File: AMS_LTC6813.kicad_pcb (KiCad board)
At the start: 2 copper layers, 205 parts, among them J1 Conn_01x06, J10 Conn_01x02_Male, J11 Conn_01x02_Male, J12 Conn_01x02_Male, J13 Conn_01x02_Male, J14 Conn_01x02_Male, J15 Conn_01x02_Male, J16 Conn_01x02_Male, J17 Conn_01x02_Male, J18 Conn_01x02_Male, J19 Conn_01x02_Male, J2 Conn_01x03_Female, J20 Conn_01x02_Male, J21 Conn_01x02_Male, J22 Conn_01x02_Male, J23 Conn_01x02_Male, J24 Conn_01x02_Male, J25 Conn_01x02_Male, J26 Conn_01x02_Male, J27 Conn_01x02_Male, J28 Conn_01x02_Male, J29 Conn_01x02_Male, J3 Conn_01x06, J30 Conn_01x02_Male, J31 Conn_01x02_Male, J32 Conn_01x02_Male, J33 Conn_01x02_Male, J34 Conn_01x02_Male, J35 Conn_01x02_Male, J36 Conn_01x02_Male, J37 Conn_01x02_Male, J38 Conn_01x02_Male, J39 Conn_01x02_Male, J4 Conn_02x02_Counter_Clockwise, J40 Conn_01x02_Male, J41 Conn_01x02_Male, J42 Conn_01x02_Male, J43 Conn_01x02_Male, J44 Conn_01x02_Male, J45 Conn_01x02_Male, J46 Conn_01x02_Male, J47 Conn_01x02_Male, J48 Conn_01x02_Male, J49 Conn_01x02_Male, J5 Conn_01x02_Male, J50 Conn_01x02_Male, J51 Conn_01x02_Male, J52 Conn_01x02_Male, J53 Conn_01x02_Male, J54 Conn_01x02_Male, J55 Conn_01x02_Male, J56 Conn_01x02_Male, J57 Conn_01x02_Male, J58 Conn_01x02_Male, J59 Conn_01x02_Male, J6 Conn_01x02_Male, J60 Conn_01x02_Male, J61 Conn_01x02_Male, J62 Conn_01x02_Male, J63 Conn_01x02_Male, J64 Conn_01x02_Male, J65 Conn_01x02_Male, J66 Conn_01x02_Male, J67 Conn_01x02_Male, J68 Conn_01x02_Male, J69 Conn_02x02_Counter_Clockwise, J7 Conn_01x02_Male, J70 Conn_01x03_Female, J71 Conn_02x20_Counter_Clockwise, J72 Conn_01x02_Male, J73 Conn_01x02_Male, J74 Conn_01x02_Male, J75 Conn_01x02_Male, J76 Conn_01x02_Male, J77 Conn_01x02_Male, J78 Conn_01x02_Male, J79 Conn_01x02_Male, J8 Conn_01x02_Male, J80 Conn_01x02_Male, J81 Conn_01x02_Male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

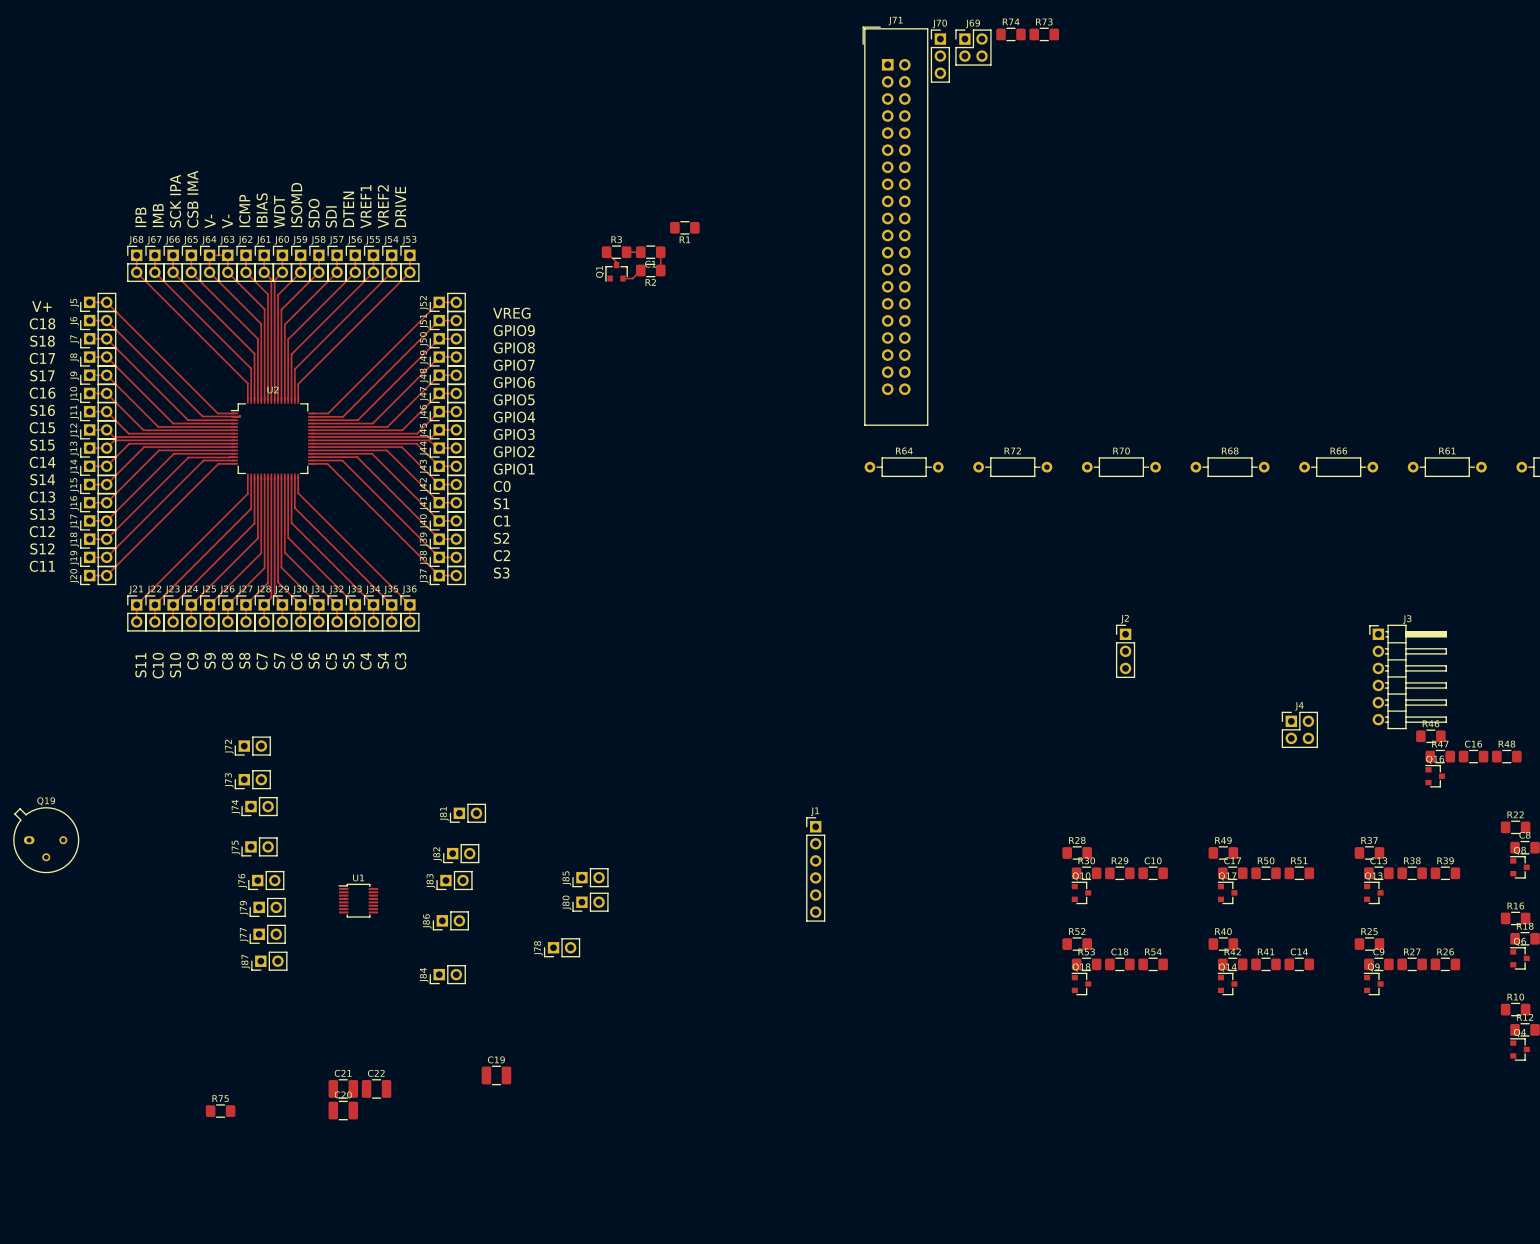
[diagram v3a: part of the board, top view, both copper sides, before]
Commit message: tout route sauf voltage channel
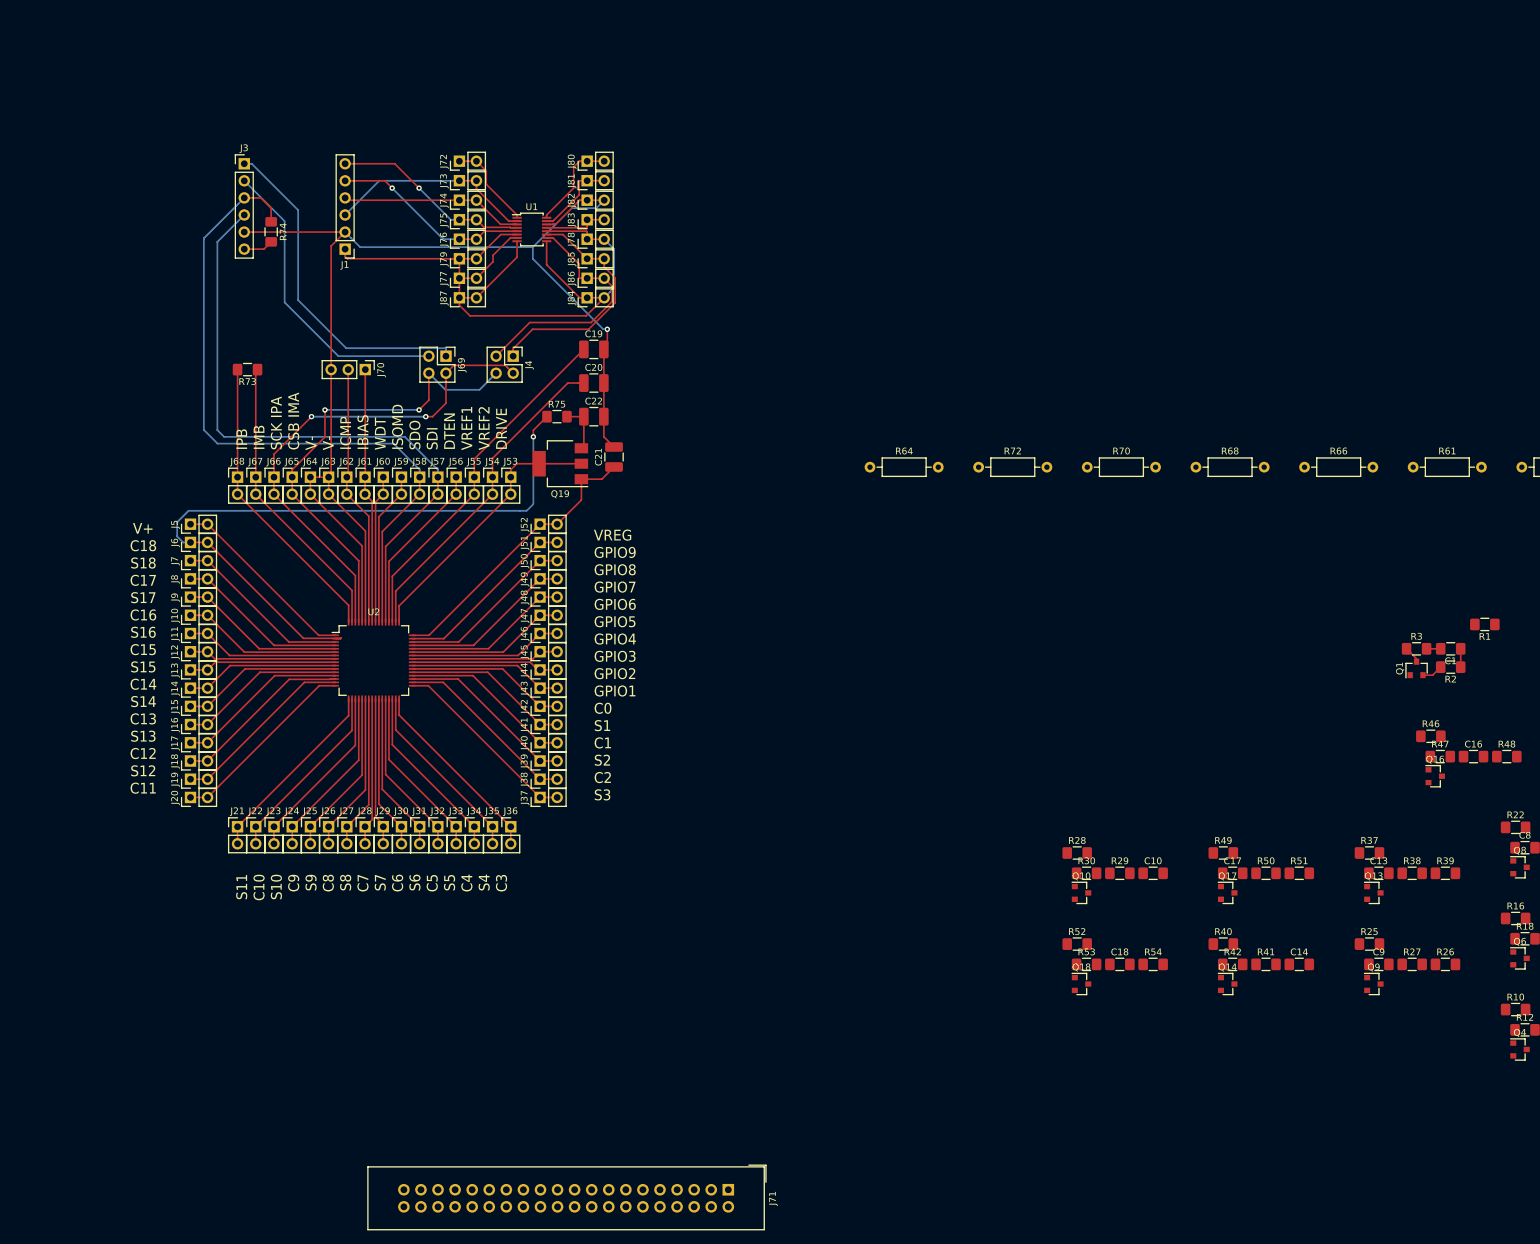
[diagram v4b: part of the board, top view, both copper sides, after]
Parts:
- removed J2: Conn_01x03_Female, Connector_PinHeader_2.54mm:PinHeader_1x03_P2.54mm_Vertical
- J3: footprint Connector_PinHeader_2.54mm:PinHeader_1x06_P2.54mm_Horizontal -> Connector_PinHeader_2.54mm:PinHeader_1x06_P2.54mm_Vertical
- Q19: footprint Package_TO_SOT_THT:TO-39-3 -> Package_TO_SOT_SMD:SOT-223-3_TabPin2
- moved J3 182.6 mm to (64.0, 32.4)
- moved J71 169.0 mm to (136.0, 185.0), turned to 270 degrees
- moved C1 132.8 mm to (243.5, 104.5)
- moved Q1 132.8 mm to (238.4, 107.5)
- moved R1 132.8 mm to (248.5, 100.9)
- moved R2 132.8 mm to (243.5, 107.3)
- moved R3 132.8 mm to (238.4, 104.5)
- moved R73 128.6 mm to (64.5, 63.0), turned to 180 degrees
- moved J4 127.9 mm to (104.0, 61.0), turned to 270 degrees
- moved R75 114.8 mm to (110.5, 70.0)
- moved C20 114.5 mm to (116.0, 65.0)
- moved R74 113.9 mm to (68.0, 42.5), turned to 270 degrees
- moved J1 110.8 mm to (79.0, 45.1), turned to 180 degrees
- moved J80 110.2 mm to (115.0, 32.0)
- moved C19 109.0 mm to (116.0, 60.0)
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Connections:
- J1 pad 6: /SCk -> /SCK
- J4 pad 1: /SCKIPA -> /IP
- J4 pad 2: /CSBIMA -> /SCKIPA
- J4 pad 4: /IP -> /CSBIMA
- J69 pad 1: /SCKIPA -> /SCKIPA1
- J69 pad 2: /CSBIMA -> /SCKIPA
- J69 pad 4: /SCKIPA1 -> /CSBIMA
- J70 pad 1: /IBIAS1 -> /IBIAS
- J70 pad 2: /ICMB1 -> /ICMP
- J70 pad 3: /GND1 -> /C0
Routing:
- net /C0: track 75.2 -> 215.6 mm, vias 0 -> 1
- net /VDD1: track 0.00 -> 117.3 mm
- net /SDO: track 23.9 -> 103.2 mm
- net /C18: track 32.0 -> 104.4 mm, vias 0 -> 1
- net /SDI: track 24.8 -> 94.8 mm
- net /SCKIPA1: track 0.00 -> 50.3 mm
- net /SCKIPA: track 26.6 -> 74.2 mm, vias 0 -> 2
- net /CSBIMA1: track 0.00 -> 45.3 mm
- net /CSBIMA: track 25.7 -> 69.8 mm, vias 0 -> 2
- net /IM: track 0.00 -> 36.8 mm
- net /IP: track 0.00 -> 36.4 mm
- net /MOSI: track 0.00 -> 30.9 mm
- net /CS: track 0.00 -> 29.7 mm, vias 0 -> 1
- net /SCK: track 0.00 -> 29.5 mm, vias 0 -> 1
- net /MISO: track 0.00 -> 27.2 mm
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
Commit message: voltages partiellements route
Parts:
- moved R59 264.6 mm to (29.0, 113.0), turned to 180 degrees
- moved R56 259.0 mm to (29.0, 97.0), turned to 180 degrees
- moved R62 257.3 mm to (59.0, 158.0), turned to 270 degrees
- moved R21 252.8 mm to (42.5, 124.6), turned to 180 degrees
- moved R55 251.7 mm to (29.0, 91.0), turned to 180 degrees
- moved C3 248.4 mm to (42.5, 99.3), turned to 180 degrees
- moved R60 247.8 mm to (29.0, 119.0), turned to 180 degrees
- moved R6 247.3 mm to (42.5, 96.5), turned to 180 degrees
- moved R65 247.1 mm to (77.0, 158.0), turned to 270 degrees
- moved C5 244.8 mm to (42.5, 110.6), turned to 180 degrees
- moved R5 244.2 mm to (51.5, 93.7), turned to 180 degrees
- moved C2 243.3 mm to (42.5, 93.7), turned to 180 degrees
- moved R58 243.2 mm to (29.0, 108.0), turned to 180 degrees
- moved C7 242.9 mm to (42.5, 121.8), turned to 180 degrees
- moved R15 239.6 mm to (42.5, 113.4), turned to 180 degrees
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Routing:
- net /C2: track 27.5 -> 76.8 mm
- net /C1: track 25.7 -> 73.0 mm
- net /C0: track 215.6 -> 236.3 mm
- net /C12: track 26.6 -> 47.1 mm
- net /C16: track 23.8 -> 43.9 mm
- net /C15: track 22.0 -> 42.1 mm
- net /C14: track 23.0 -> 43.0 mm
- net /C17: track 27.8 -> 45.8 mm
- net /C13: track 24.8 -> 42.1 mm
- net /C3: track 28.4 -> 42.6 mm
- net Net-(Q15-Pad3): track 0.00 -> 11.1 mm
- net Net-(Q18-Pad3): track 0.00 -> 10.7 mm
- net /C18: track 104.4 -> 114.9 mm
- net Net-(Q17-Pad3): track 0.00 -> 10.5 mm
- net /CELL3: track 0.00 -> 3.75 mm
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
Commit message: routing everything
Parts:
- moved J71 82.0 mm to (54.6, 175.3), turned to 90 degrees
- moved R61 33.5 mm to (38.1, 157.5), turned to 270 degrees
- moved R60 27.3 mm to (38.1, 144.8), turned to 270 degrees
- moved C18 23.2 mm to (98.8, 152.2)
- moved R72 23.1 mm to (101.8, 156.7)
- moved R54 23.1 mm to (101.8, 152.2)
- moved C15 23.0 mm to (104.9, 152.2)
- moved R45 23.0 mm to (108.0, 152.2)
- moved R69 23.0 mm to (108.0, 156.7)
- moved Q15 22.9 mm to (106.9, 147.5)
- moved R43 22.9 mm to (108.0, 143.2)
- moved R44 22.7 mm to (104.9, 143.2)
- moved R52 22.6 mm to (101.8, 143.2)
- moved Q18 22.6 mm to (100.7, 147.5)
- moved R53 22.5 mm to (98.8, 143.2)
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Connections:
- J71 pad 10: /CELL10 -> /CELL14
- J71 pad 11: /CELL9 -> Net-(J71-Pad11)
- J71 pad 12: /CELL8 -> /CELL13
- J71 pad 13: /CELL7 -> Net-(J71-Pad13)
- J71 pad 14: /CELL6 -> /CELL12
- J71 pad 15: /CELL5 -> Net-(J71-Pad15)
- J71 pad 16: /CELL4 -> /CELL11
- J71 pad 17: /CELL3 -> Net-(J71-Pad17)
- J71 pad 18: /CELL2 -> /CELL10
- J71 pad 19: /CELL1 -> Net-(J71-Pad19)
- J71 pad 20: /C0 -> /CELL9
- J71 pad 21: /GPIO1 -> Net-(J71-Pad21)
- J71 pad 22: /GPIO2 -> /CELL8
- J71 pad 23: /GPIO3 -> /GPIO9
- J71 pad 24: /GPIO4 -> /CELL7
- J71 pad 25: /GPIO5 -> /GPIO8
- J71 pad 26: /GPIO6 -> /CELL6
- J71 pad 28: /GPIO8 -> /CELL5
- J71 pad 29: /GPIO9 -> /GPIO6
- J71 pad 3: /CELL17 -> Net-(J71-Pad3)
- J71 pad 30: Net-(J71-Pad30) -> /CELL4
- J71 pad 31: Net-(J71-Pad31) -> /GPIO5
- J71 pad 32: Net-(J71-Pad32) -> /CELL3
- J71 pad 33: Net-(J71-Pad33) -> /GPIO4
- J71 pad 34: Net-(J71-Pad34) -> /CELL2
- J71 pad 35: Net-(J71-Pad35) -> /GPIO3
- J71 pad 36: Net-(J71-Pad36) -> /CELL1
- J71 pad 37: Net-(J71-Pad37) -> /GPIO2
- J71 pad 38: Net-(J71-Pad38) -> /C0
- J71 pad 39: Net-(J71-Pad39) -> /GPIO1
- J71 pad 4: /CELL16 -> /CELL17
- J71 pad 5: /CELL15 -> Net-(J71-Pad5)
- J71 pad 6: /CELL14 -> /CELL16
- J71 pad 7: /CELL13 -> Net-(J71-Pad7)
- J71 pad 8: /CELL12 -> /CELL15
- J71 pad 9: /CELL11 -> Net-(J71-Pad9)
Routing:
- net /GPIO9: track 27.5 -> 144.0 mm
- net /GPIO8: track 26.6 -> 136.7 mm
- net /GPIO7: track 25.7 -> 129.4 mm
- net /GPIO5: track 23.8 -> 121.5 mm
- net /GPIO6: track 24.7 -> 122.1 mm
- net /CELL18: track 2.29 -> 97.1 mm, vias 0 -> 1
- net /GPIO4: track 22.9 -> 114.2 mm
- net /CELL17: track 2.26 -> 92.7 mm, vias 0 -> 1
- net /GPIO3: track 22.0 -> 106.9 mm
- net /CELL16: track 2.24 -> 86.3 mm, vias 0 -> 1
- net /CELL15: track 2.21 -> 82.1 mm, vias 0 -> 1
- net /GPIO2: track 22.0 -> 100.6 mm
- net /CELL14: track 2.18 -> 74.1 mm, vias 0 -> 1
- net /GPIO1: track 23.0 -> 93.8 mm
- net /CELL13: track 2.16 -> 69.6 mm, vias 0 -> 1
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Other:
- board outline added: 94 x 165.2 mm
